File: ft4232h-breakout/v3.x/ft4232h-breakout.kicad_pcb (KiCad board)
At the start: 2 copper layers, 81 x 55.6 mm, 0 parts

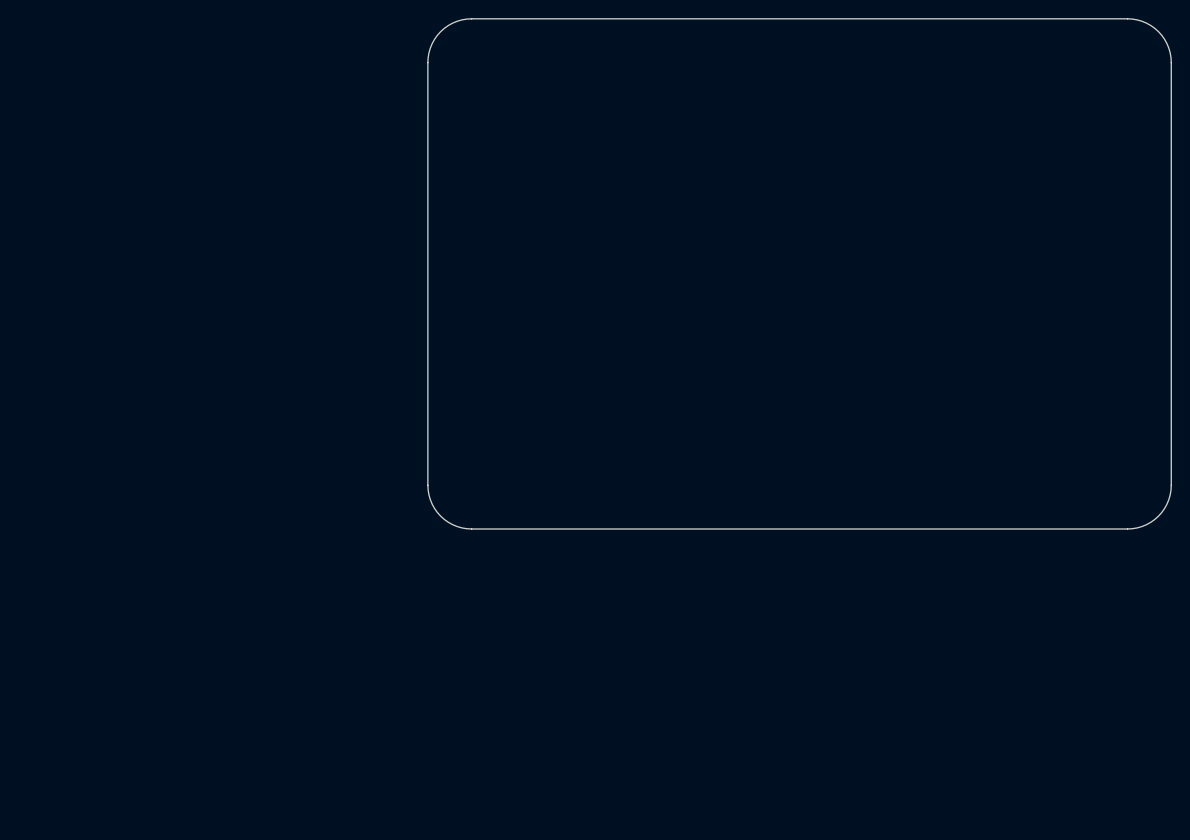
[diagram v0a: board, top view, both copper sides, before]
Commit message: ft4232h-breakout: v3 at rc1
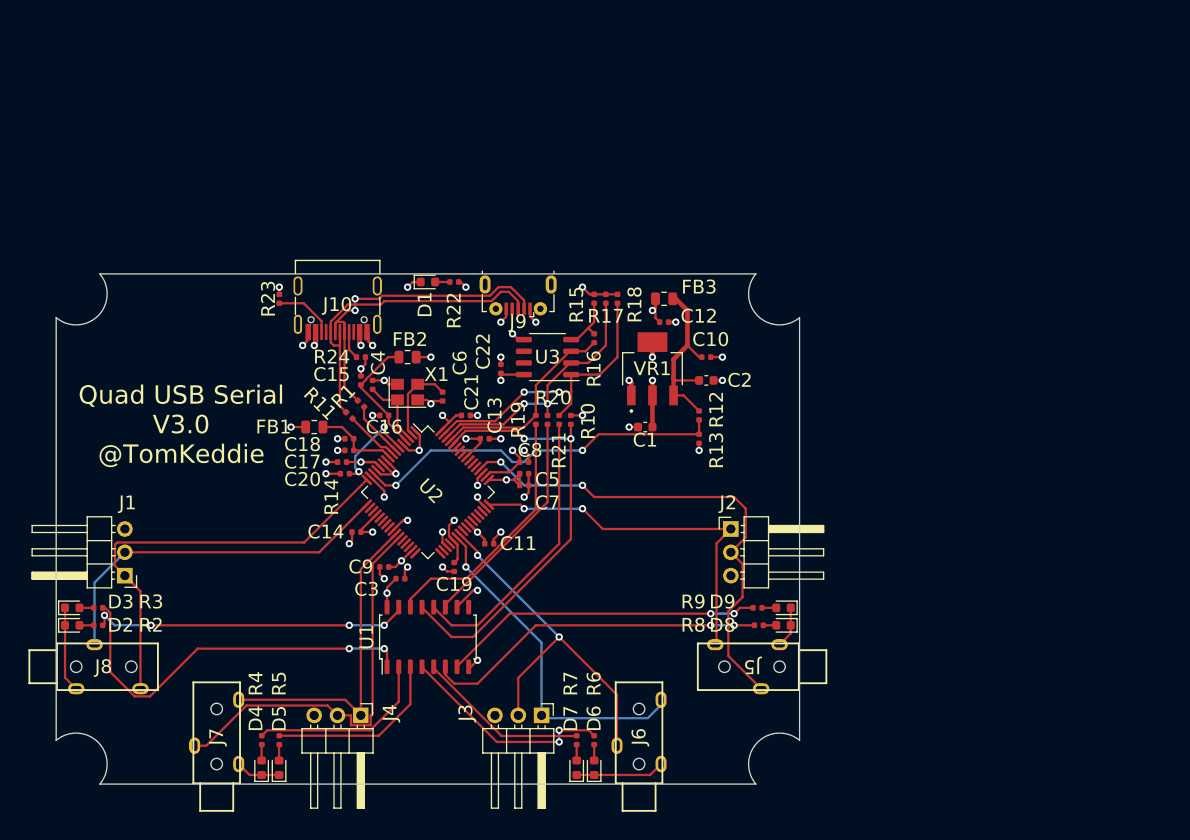
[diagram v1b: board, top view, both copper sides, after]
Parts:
- added C1: 10uF_10V_X5R, tom-passives:C_0603_1608Metric, F.Cu at (123.7, 88.9)
- added C10: 100nF_50V_X7R, tom-passives:C_0402_1005Metric, F.Cu at (130.3, 81.3)
- added C11: 100nF_50V_X7R, tom-passives:C_0402_1005Metric, F.Cu at (106.7, 101.6)
- added C12: 10nF_50V_X7R, tom-passives:C_0402_1005Metric, F.Cu at (125.7, 77.5)
- added C13: 100nF_50V_X7R, tom-passives:C_0402_1005Metric, F.Cu at (106.2, 90.2)
- added C14: 100nF_50V_X7R, tom-passives:C_0402_1005Metric, F.Cu at (92.2, 100.3)
- added C15: 4.7uF_10V_X5R, tom-passives:C_0402_1005Metric, F.Cu at (92.7, 83.8)
- added C16: 100nF_50V_X7R, tom-passives:C_0402_1005Metric, F.Cu at (95.2, 87.6)
- added C17: 4.7uF_10V_X5R, tom-passives:C_0402_1005Metric, F.Cu at (91.4, 90.2)
- added C18: 100nF_50V_X7R, tom-passives:C_0402_1005Metric, F.Cu at (91.4, 91.4)
- added C19: 100nF_50V_X7R, tom-passives:C_0402_1005Metric, F.Cu at (102.9, 104.1)
- added C2: 10uF_10V_X5R, tom-passives:C_0603_1608Metric, F.Cu at (130.3, 83.8)
- added C20: 100nF_50V_X7R, tom-passives:C_0402_1005Metric, F.Cu at (90.7, 92.7)
- added C21: 100nF_50V_X7R, tom-passives:C_0402_1005Metric, F.Cu at (104.1, 87.6)
- added C22: 100nF_50V_X7R, tom-passives:C_0402_1005Metric, F.Cu at (108.0, 82.5)
- added C3: 100nF_50V_X7R, tom-passives:C_0402_1005Metric, F.Cu at (97.0, 105.4)
- added C4: 20pF_50V_C0G, tom-passives:C_0402_1005Metric, F.Cu at (94.0, 84.3)
- added C5: 4.7uF_10V_X5R, tom-passives:C_0402_1005Metric, F.Cu at (110.5, 94.0)
- added C6: 20pF_50V_C0G, tom-passives:C_0402_1005Metric, F.Cu at (101.6, 85.6)
- added C7: 100nF_50V_X7R, tom-passives:C_0402_1005Metric, F.Cu at (110.5, 95.2)
- added C8: 100nF_50V_X7R, tom-passives:C_0402_1005Metric, F.Cu at (110.5, 92.7)
- added C9: 100nF_50V_X7R, tom-passives:C_0402_1005Metric, F.Cu at (95.2, 104.1)
- added D1: LED, tom-opto:LED_0603_1608Metric, F.Cu at (100.0, 73.1)
- added D2: TXA, tom-opto:LED_0603_1608Metric, F.Cu at (61.3, 110.5)
- added D3: RXA, tom-opto:LED_0603_1608Metric, F.Cu at (61.3, 108.6)
- added D4: TXB, tom-opto:LED_0603_1608Metric, F.Cu at (81.9, 126.0)
- added D5: RXB, tom-opto:LED_0603_1608Metric, F.Cu at (83.8, 126.0)
- added D6: TXC, tom-opto:LED_0603_1608Metric, F.Cu at (118.1, 126.0)
- added D7: RXC, tom-opto:LED_0603_1608Metric, F.Cu at (116.2, 126.0)
- added D8: TXD, tom-opto:LED_0603_1608Metric, F.Cu at (138.7, 110.5)
- added D9: RXD, tom-opto:LED_0603_1608Metric, F.Cu at (138.7, 108.6)
- added FB1: 500mA/600R, tom-passives:C_0805_2012Metric, F.Cu at (87.6, 88.9)
- added FB2: 500mA/600R, tom-passives:C_0805_2012Metric, F.Cu at (97.8, 81.3)
- added FB3: 500mA/600R, tom-passives:C_0805_2012Metric, F.Cu at (125.7, 74.9)
- added J1: Conn_01x03, tom-connectors:PinHeader_1x03_P2.54mm_Horizontal, F.Cu at (67.0, 105.1)
- added J10: USB_C_Receptacle_USB2.0, tom-connectors:USB_C_Receptacle_LCSC_C165948, F.Cu at (90.2, 75.4)
- added J2: Conn_01x03, tom-connectors:PinHeader_1x03_P2.54mm_Horizontal, F.Cu at (133.0, 100.0)
- added J3: Conn_01x03, tom-connectors:PinHeader_1x03_P2.54mm_Horizontal, F.Cu at (112.4, 120.3)
- added J4: Conn_01x03, tom-connectors:PinHeader_1x03_P2.54mm_Horizontal, F.Cu at (92.7, 120.3)
- added J5: JLCPCB_3.5MM_SOCKET_C18166, tom-connectors:JLCPCB_3.5MM_SOCKET_C18166, F.Cu at (140.4, 115.0)
- added J6: JLCPCB_3.5MM_SOCKET_C18166, tom-connectors:JLCPCB_3.5MM_SOCKET_C18166, F.Cu at (123.0, 127.7)
- added J7: JLCPCB_3.5MM_SOCKET_C18166, tom-connectors:JLCPCB_3.5MM_SOCKET_C18166, F.Cu at (77.0, 127.7)
- added J8: JLCPCB_3.5MM_SOCKET_C18166, tom-connectors:JLCPCB_3.5MM_SOCKET_C18166, F.Cu at (59.6, 115.0)
- added J9: USB_B_Micro, tom-connectors:USB_B_Micro_LCSC_C10418, F.Cu at (109.8, 71.6)
- added R1: 10, tom-passives:R_0402_1005Metric, F.Cu at (92.7, 86.4)
- added R10: 10k, tom-passives:R_0402_1005Metric, F.Cu at (115.6, 88.1)
- added R11: 10, tom-passives:R_0402_1005Metric, F.Cu at (91.4, 87.6)
- added R12: 15k, tom-passives:R_0402_1005Metric, F.Cu at (129.5, 87.6)
- added R13: 10k, tom-passives:R_0402_1005Metric, F.Cu at (129.5, 90.2)
- added R14: 12k, tom-passives:R_0402_1005Metric, F.Cu at (91.0, 94.0)
- added R15: 10k, tom-passives:R_0402_1005Metric, F.Cu at (118.1, 74.9)
- added R16: 2.2k, tom-passives:R_0402_1005Metric, F.Cu at (118.1, 79.2)
- added R17: 10k, tom-passives:R_0402_1005Metric, F.Cu at (119.4, 74.9)
- added R18: 10k, tom-passives:R_0402_1005Metric, F.Cu at (120.7, 74.9)
- added R19: 0, tom-passives:R_0402_1005Metric, F.Cu at (111.8, 88.1)
- added R2: 330, tom-passives:R_0402_1005Metric, F.Cu at (64.1, 110.5)
- added R20: 0, tom-passives:R_0402_1005Metric, F.Cu at (113.0, 88.1)
- added R21: 0, tom-passives:R_0402_1005Metric, F.Cu at (114.3, 88.1)
- added R22: 330, tom-passives:R_0402_1005Metric, F.Cu at (102.9, 73.1)
- added R23: 5.1k, tom-passives:R_0402_1005Metric, F.Cu at (83.8, 74.9)
- added R24: 5.1k, tom-passives:R_0402_1005Metric, F.Cu at (92.7, 81.3)
- added R3: 330, tom-passives:R_0402_1005Metric, F.Cu at (64.1, 108.6)
- added R4: 330, tom-passives:R_0402_1005Metric, F.Cu at (81.9, 123.0)
- added R5: 330, tom-passives:R_0402_1005Metric, F.Cu at (83.8, 123.0)
- added R6: 330, tom-passives:R_0402_1005Metric, F.Cu at (118.1, 123.0)
- added R7: 330, tom-passives:R_0402_1005Metric, F.Cu at (116.2, 123.0)
- added R8: 330, tom-passives:R_0402_1005Metric, F.Cu at (136.0, 110.5)
- added R9: 330, tom-passives:R_0402_1005Metric, F.Cu at (135.9, 108.6)
- added U1: 74HC595, tom-semiconductors:SOIC-16_4.55x10.3mm_P1.27mm, F.Cu at (100.0, 111.8)
- added U2: FT4232H, tom-semiconductors:TQFP-64_10x10mm_P0.5mm, F.Cu at (100.0, 96.0)
- added U3: AT93C46DN-SH-T, tom-semiconductors:SO-8_3.9x4.9mm_P1.27mm, F.Cu at (113.0, 81.3)
- added VR1: LM1117MPX-3.3, tom-semiconductors:VREG_LM1117MPX-3.3, F.Cu at (124.5, 82.5)
- added X1: 12MHz, tom-passives:Crystal_SMD_3225-4Pin_3.2x2.5mm, F.Cu at (97.8, 85.1)
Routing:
- net GND: track 0.00 -> 96.7 mm, vias 0 -> 38
- net /RXD-D: track 0.00 -> 54.4 mm, vias 0 -> 2
- net /VUSB: track 0.00 -> 51.1 mm, vias 0 -> 4
- net VCORE: track 0.00 -> 49.2 mm, vias 0 -> 4
- net /~{PWREN}: track 0.00 -> 48.3 mm, vias 0 -> 2
- net /TXD-A: track 0.00 -> 47.2 mm
- net VCCIO: track 0.00 -> 46.4 mm, vias 0 -> 15
- net /RXD-B: track 0.00 -> 44.3 mm
- net Net-(R3-Pad1): track 0.00 -> 42.7 mm, vias 0 -> 2
- net /~{RESET}: track 0.00 -> 41.0 mm, vias 0 -> 2
- net /TXD-D: track 0.00 -> 40.7 mm, vias 0 -> 2
- net /RXD-C: track 0.00 -> 40.5 mm, vias 0 -> 2
- net /RXD-A: track 0.00 -> 39.9 mm
- net Net-(R8-Pad1): track 0.00 -> 37.6 mm, vias 0 -> 2
- net /TXD-C: track 0.00 -> 37.5 mm, vias 0 -> 1
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- added copper zone on In1.Cu, net GND
- added copper zone on In2.Cu, net VCCIO
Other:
- copper layers 2 -> 4
- board text added: "Digikey 1722-1013-ND"
- board text added: "Quad USB Serial V3.0 @TomKeddie"

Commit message: ft4232h-breakout: v3.0 as submitted to jlcpcb for pcb run
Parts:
- moved C13 1.14 mm to (106.7, 91.2)
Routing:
- net VCCIO: track 46.4 -> 176.3 mm, vias 15 -> 6
- net /~{RESET}: track 41.0 -> 78.0 mm, vias 2 -> 4
- net GND: track 96.7 -> 93.1 mm, vias 38 -> 39
- net Net-(R6-Pad1): track 23.7 -> 25.3 mm
- net /EECLK: track 28.5 -> 29.3 mm
- net Net-(R14-Pad2): track 10.4 -> 9.84 mm
- net /VUSB: track 51.1 -> 51.5 mm, vias 4 -> 2
- added copper zone on B.Cu, net GND
- added copper zone on F.Cu, net GND
- removed copper zone on In1.Cu, net GND
- removed copper zone on In2.Cu, net VCCIO
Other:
- copper layers 4 -> 2

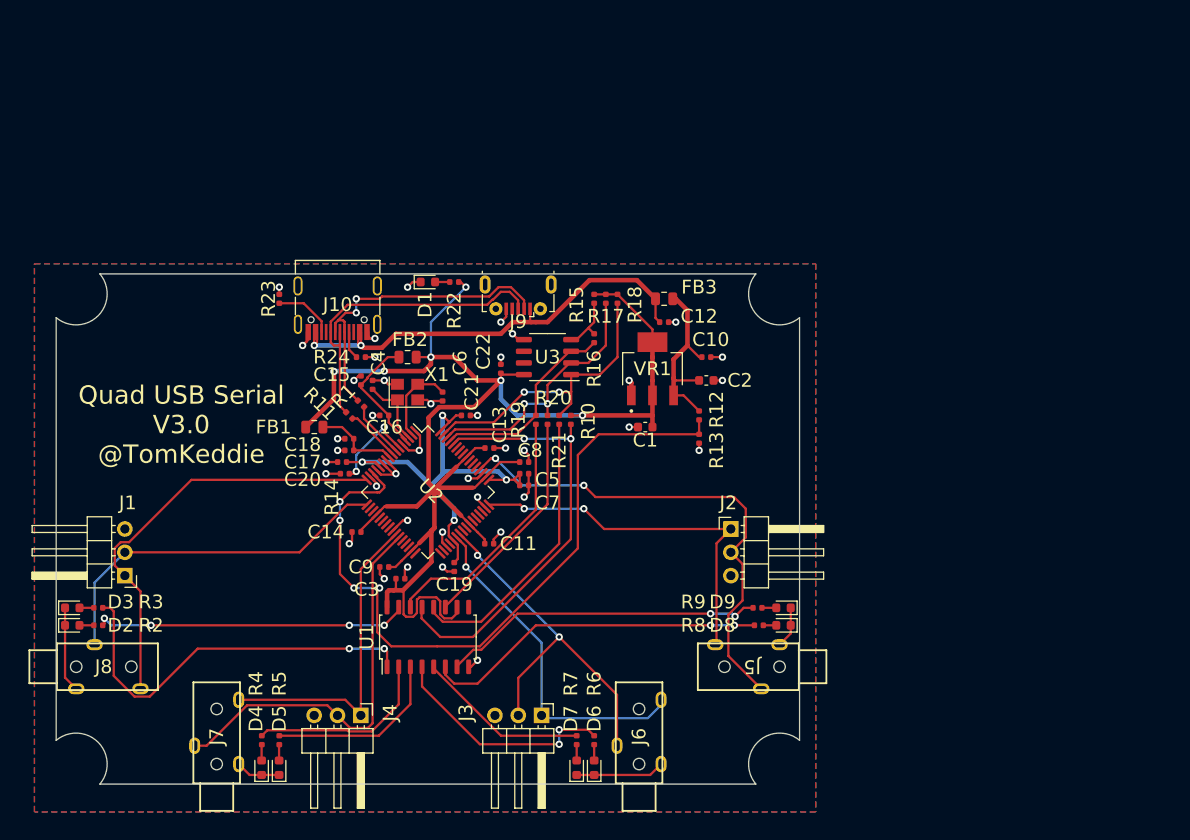
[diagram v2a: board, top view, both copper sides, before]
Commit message: ft4232h-breakout: updates for v3.1
- fixed mount hole sizes
- fixed exterior dimensions
- updated rev on silk
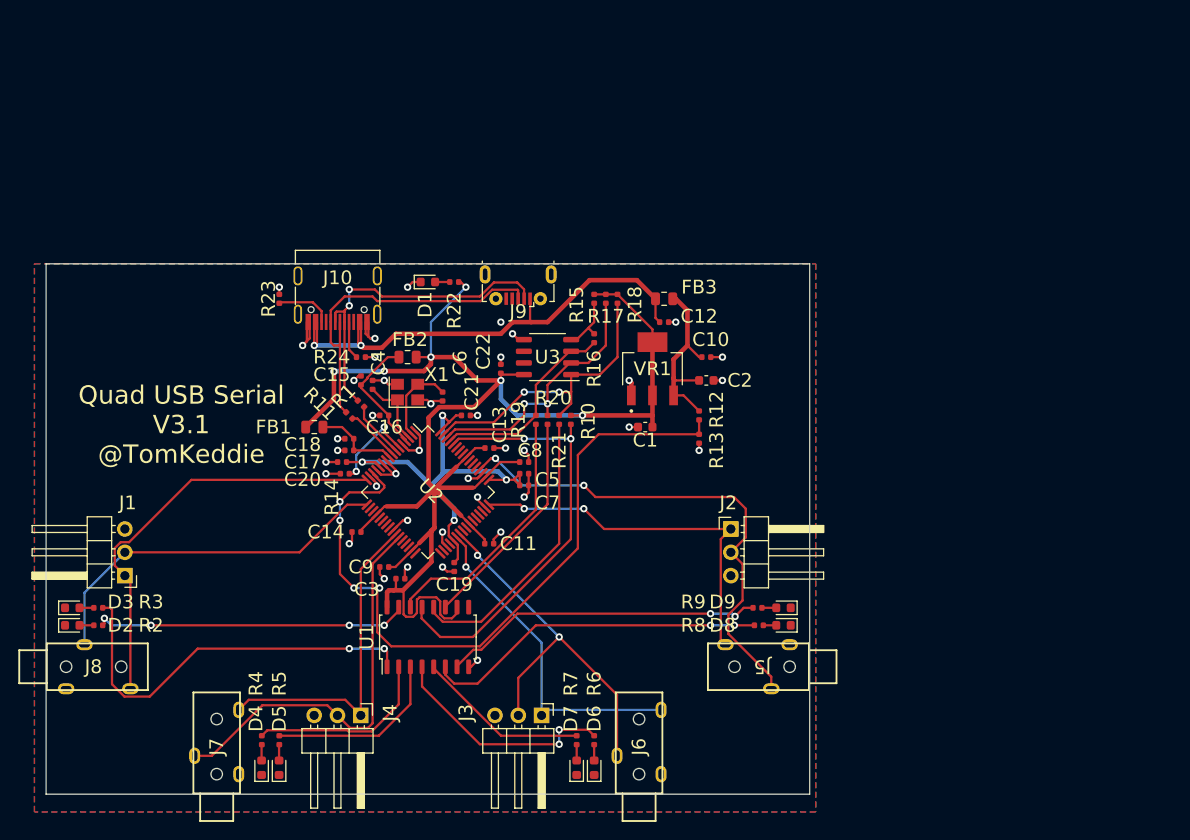
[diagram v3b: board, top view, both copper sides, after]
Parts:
- moved J10 1.10 mm to (90.2, 74.3)
- moved J6 1.10 mm to (123.0, 128.8)
- moved J7 1.10 mm to (77.0, 128.8)
- moved J9 1.10 mm to (109.8, 70.5)
- moved J8 1.10 mm to (58.5, 115.0)
- moved J5 1.10 mm to (141.5, 115.0)
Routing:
- net GND: track 93.1 -> 68.0 mm
- net /VUSB: track 51.5 -> 57.0 mm
- net /USB_P: track 35.5 -> 37.5 mm
- net /RXD-C: track 40.5 -> 41.6 mm
- net Net-(J10-PadA5): track 3.06 -> 4.16 mm
- net /TXD-C: track 37.5 -> 36.5 mm
- net Net-(R3-Pad1): track 43.1 -> 43.7 mm
- net /USB_N: track 35.6 -> 36.3 mm
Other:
- board size 81 x 55.6 mm -> 83.2 x 57.8 mm
- board text added: "Quad USB Serial V3.1 @TomKeddie"
- board text added: "X size 3.51{dblquote} = 89.154mm - 2*3mm = 83 mm"
- board text added: "Y size 2.51{dblquote} = 63.754 - 2 * 3mm = 57.75"
- board text removed: "Quad USB Serial V3.0 @TomKeddie"
